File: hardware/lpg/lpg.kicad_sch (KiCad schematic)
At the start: 66 parts, among them J1 AudioJack2_SwitchT, J2 AudioJack2_SwitchT, J3 AudioJack2_SwitchT, J4 AudioJack2_SwitchT, J5 Conn_02x05_Odd_Even, Q1 BC547, Q2 BC547, SW1 SW_3PDT_x3, SW2 SW_DPDT_x2, U1 TL074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

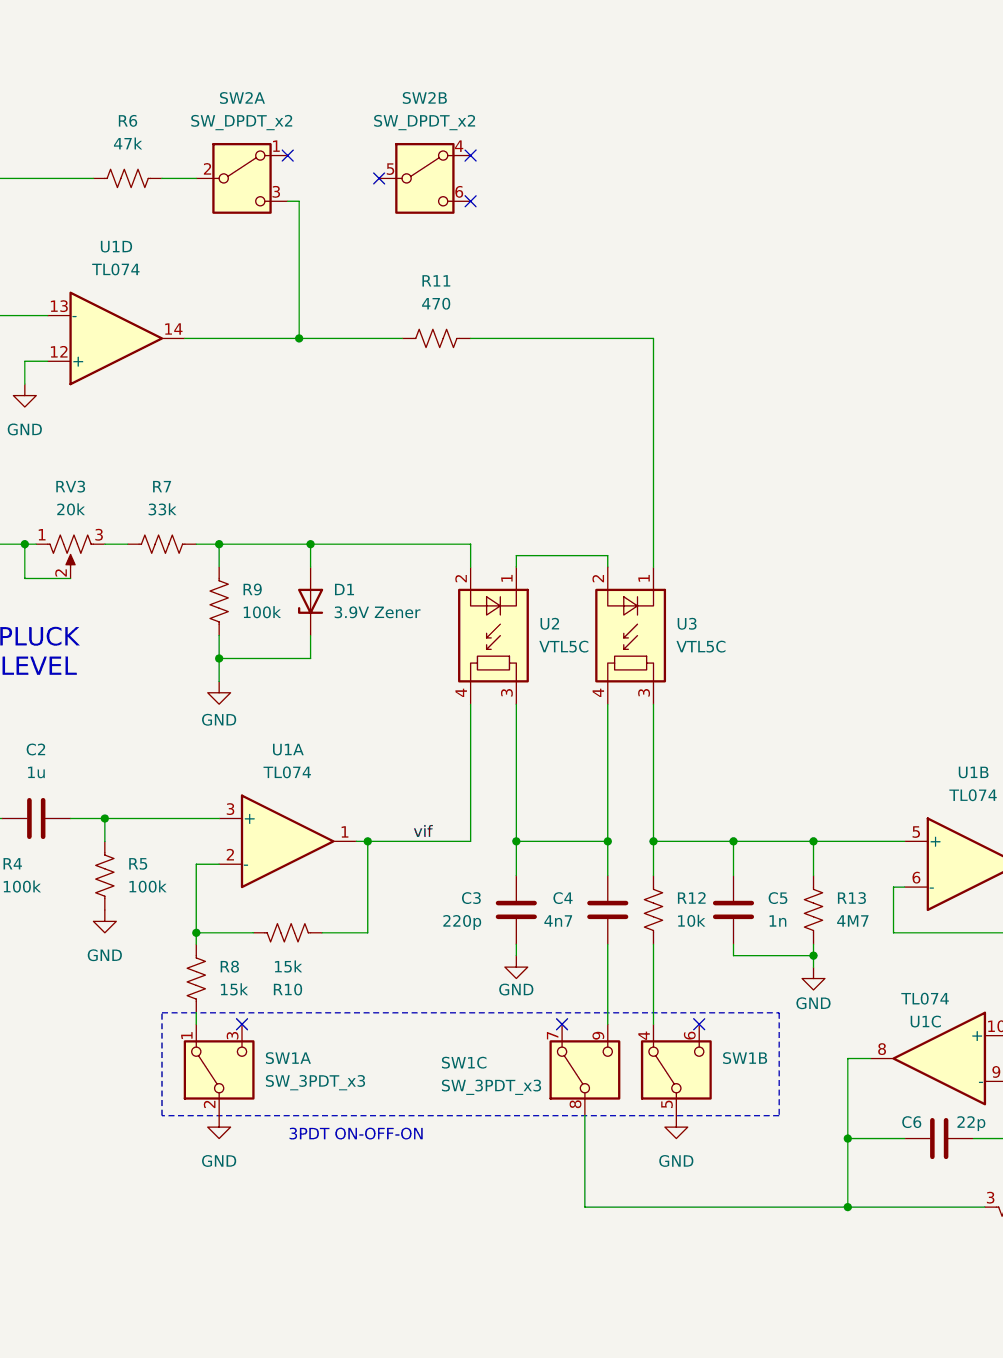
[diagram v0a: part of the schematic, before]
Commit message: replaced switches with 4P3T slider and SPDT M5 sub-mini toggle
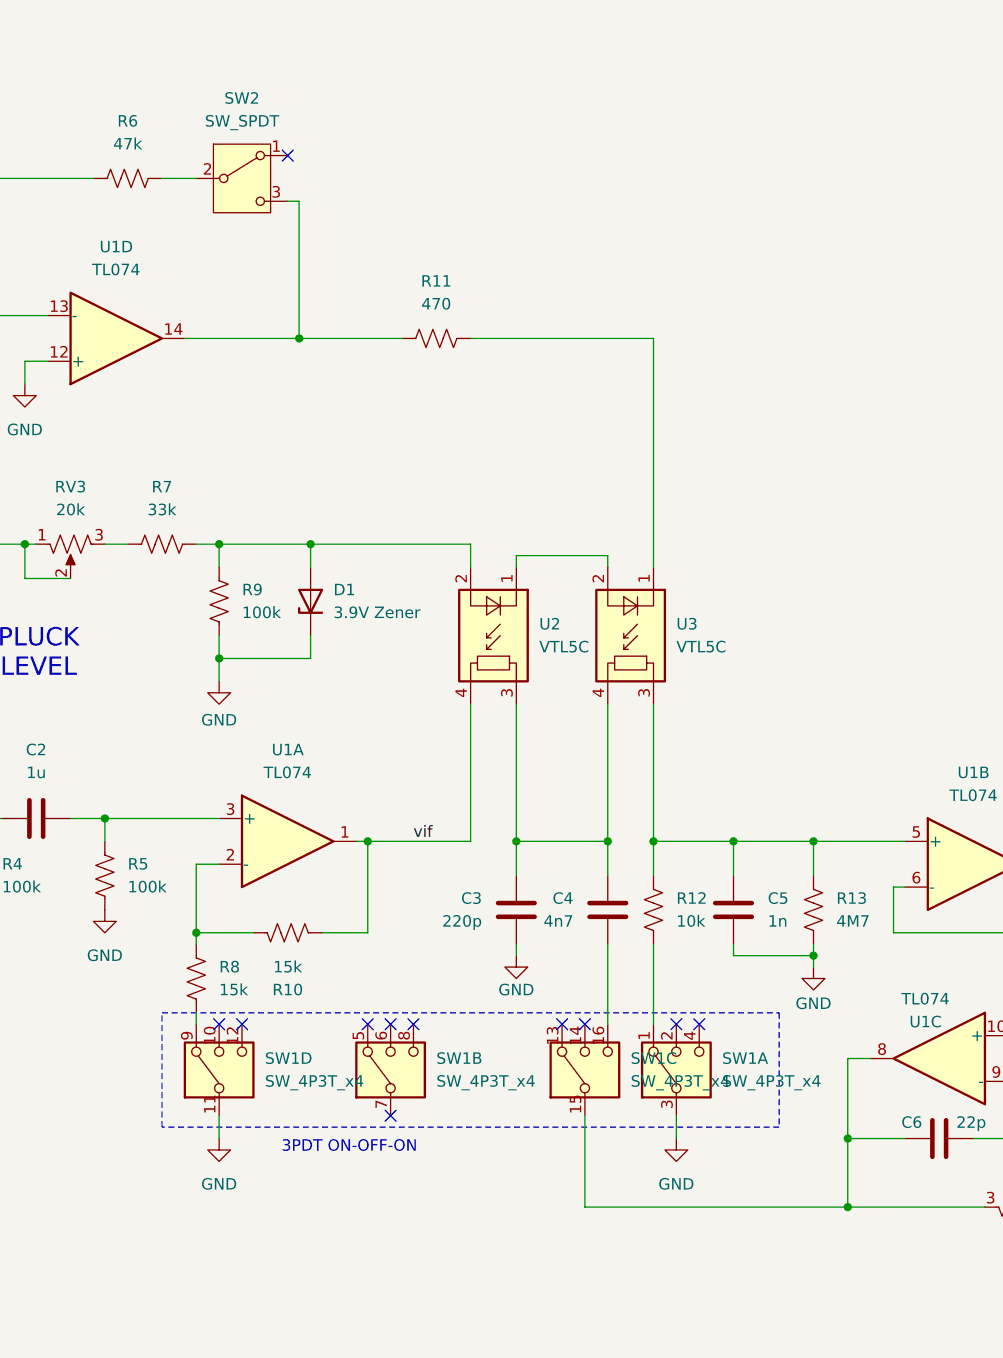
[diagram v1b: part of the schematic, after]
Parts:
- removed SW1: SW_3PDT_x3, Switches:SW_3PDT_18mm_x_13mm_P4.50mm, symbol Modular_Switches:SW_3PDT_x3
- removed SW2: SW_DPDT_x2, Switches:SW_DPDT_13mm_x_13mm_P5.00mm, symbol Switch:SW_DPDT_x2
- added SW1: SW_4P3T_x4, Switches:SW_4P3T_SS-43D01_NoFrame, symbol Modular_Switches:SW_4P3T_x4
- added SW2: SW_SPDT, Switches:SW_Dailywell_SPDT_2MS1T1B1M1, symbol Switch:SW_SPDT
- C5: footprint Capacitor_THT:C_Disc_D5.0mm_W2.5mm_P2.50mm -> Capacitor_THT:C_Disc_D5.0mm_W2.5mm_P5.00mm
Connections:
- net GND: now also SW1.11, SW1.3
- net at C4.1: now also SW1.16
- net at C6.2, RV4.3, U1.8: now also SW1.15
- net at R11.2, U1.14: now also SW2.3 (C)
- net at R8.2: now also SW1.9
- net at R12.2: now also SW1.1
- net at R6.1: now also SW2.2 (B)
- no-connect marks 11 -> 15

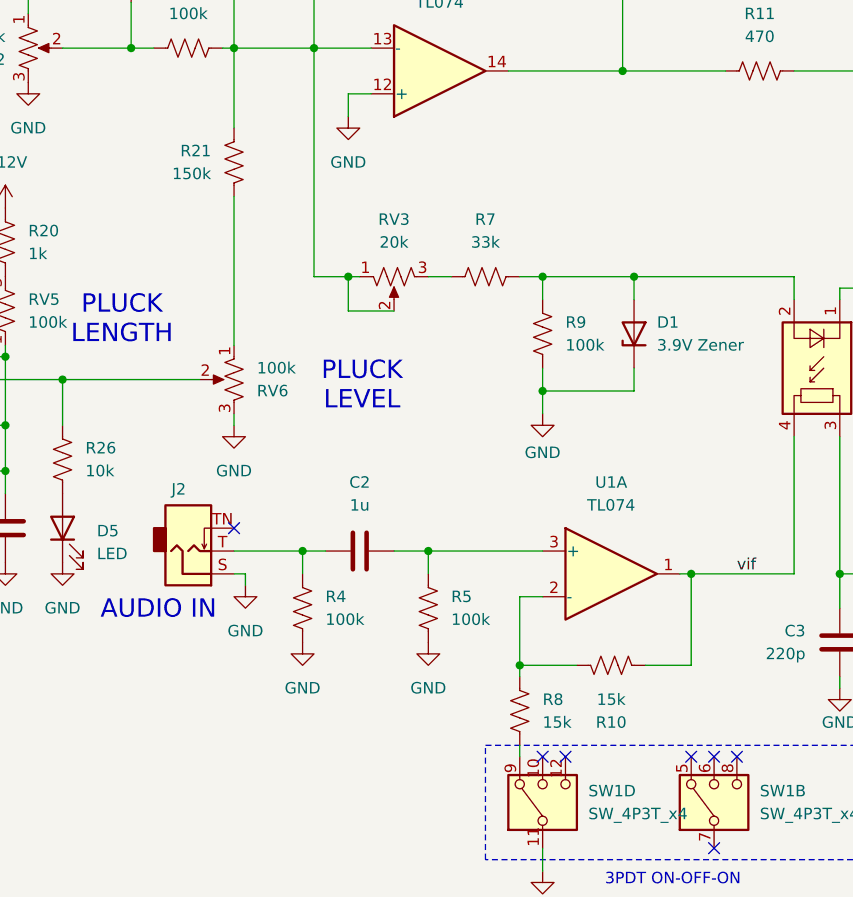
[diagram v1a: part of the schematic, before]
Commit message: Faceplate layout and silkscreen
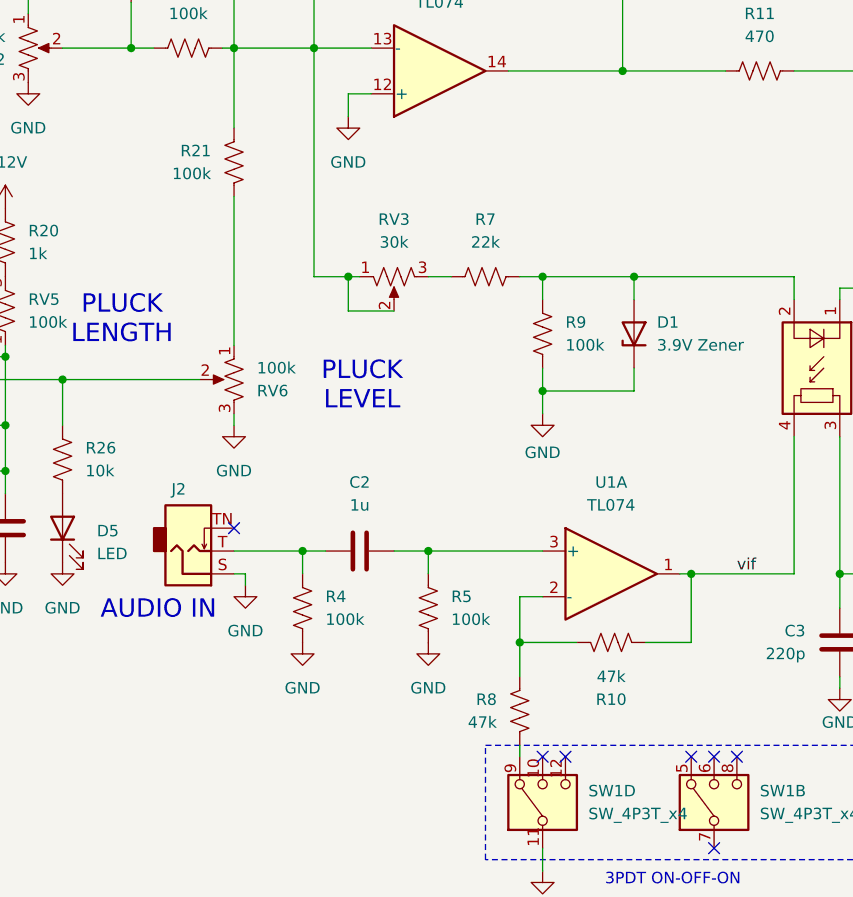
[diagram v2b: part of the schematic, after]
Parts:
- R10, R8: value 15k -> 47k
- R21: value 150k -> 100k
- R7: value 33k -> 22k
- RV3: value 20k -> 30k
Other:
- moved on the sheet: R10
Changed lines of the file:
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@@
 	)
 	(junction
+		(at 160.02 111.76)
+		(diameter 0)
+		(color 0 0 0 0)
+	)
+	(junction
 		(at 102.87 87.63)
 		(diameter 0)
@@
 	)
 	(junction
-		(at 160.02 114.3)
-		(diameter 0)
-		(color 0 0 0 0)
-	)
-	(junction
 		(at 90.17 154.94)
 		(diameter 0)
@@
 	(wire
 		(pts
-			(xy 160.02 114.3) (xy 160.02 115.57)
+			(xy 160.02 111.76) (xy 160.02 115.57)
 		)
 		(stroke
@@
 	(wire
 		(pts
-			(xy 160.02 114.3) (xy 166.37 114.3)
+			(xy 160.02 111.76) (xy 166.37 111.76)
 		)
 		(stroke
@@
 	(wire
 		(pts
-			(xy 179.07 114.3) (xy 179.07 104.14)
+			(xy 179.07 111.76) (xy 179.07 104.14)
 		)
 		(stroke
@@
 	(wire
 		(pts
-			(xy 160.02 106.68) (xy 160.02 114.3)
+			(xy 160.02 106.68) (xy 160.02 111.76)
 		)
 		(stroke
@@
 	(wire
 		(pts
-			(xy 173.99 114.3) (xy 179.07 114.3)
+			(xy 173.99 111.76) (xy 179.07 111.76)
 		)
 		(stroke
@@
 	(symbol
 		(lib_id "Device:R_US")
-		(at 170.18 114.3 90)
+		(at 170.18 111.76 90)
 		(mirror x)
 		(unit 1)
@@
 		(dnp no)
 		(property "Reference" "R10"
-			(at 170.18 120.65 90)
+			(at 170.18 118.11 90)
 			(effects
 				(font
@@
 			)
 		)
-		(property "Value" "15k"
-			(at 170.18 118.11 90)
+		(property "Value" "47k"
+			(at 170.18 115.57 90)
 			(effects
 				(font
@@
 		)
 		(property "Footprint" "Resistor_THT:R_Axial_DIN0204_L3.6mm_D1.6mm_P2.54mm_Vertical"
-			(at 170.434 115.316 90)
+			(at 170.434 112.776 90)
 			(effects
 				(font
@@
 		)
 		(property "Datasheet" "~"
-			(at 170.18 114.3 0)
+			(at 170.18 111.76 0)
 			(effects
 				(font
@@
 		)
 		(property "Description" "Resistor, US symbol"
-			(at 170.18 114.3 0)
+			(at 170.18 111.76 0)
 			(effects
 				(font
@@
 		(lib_id "Device:R_US")
 		(at 160.02 119.38 0)
+		(mirror y)
 		(unit 1)
 		(exclude_from_sim no)
@@
 		(on_board yes)
 		(dnp no)
-		(fields_autoplaced yes)
 		(property "Reference" "R8"
-			(at 162.56 118.1099 0)
+			(at 157.48 118.1099 0)
 			(effects
 				(font
@@
 			)
 		)
-		(property "Value" "15k"
-			(at 162.56 120.6499 0)
+		(property "Value" "47k"
+			(at 157.48 120.6499 0)
 			(effects
 				(font
@@
 		)
 		(property "Footprint" "Resistor_THT:R_Axial_DIN0204_L3.6mm_D1.6mm_P2.54mm_Vertical"
-			(at 161.036 119.634 90)
+			(at 159.004 119.634 90)
 			(effects
 				(font
@@
 			)
 		)
-		(property "Value" "150k"
+		(property "Value" "100k"
 			(at 125.73 59.6899 0)
 			(effects
@@
 			)
 		)
-		(property "Value" "20k"
+		(property "Value" "30k"
 			(at 146.05 67.31 90)
 			(effects
@@
 			)
 		)
-		(property "Value" "33k"
+		(property "Value" "22k"
 			(at 156.21 67.31 90)
 			(effects

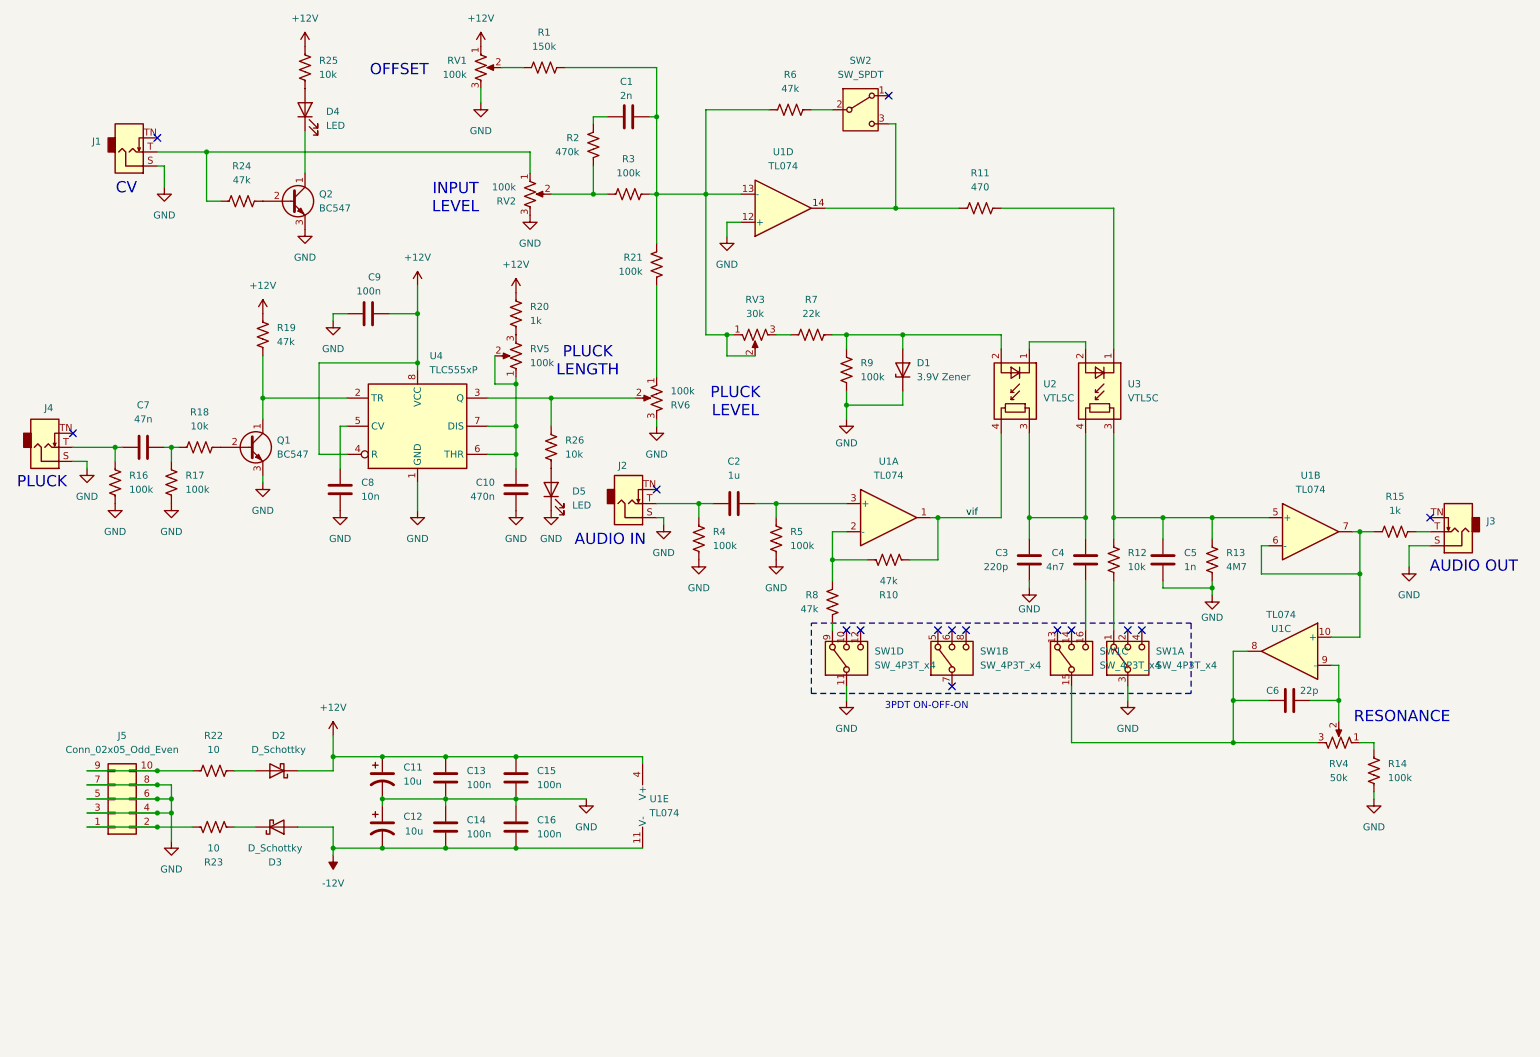
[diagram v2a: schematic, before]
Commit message: Update KiCad project settings and error handling parameters
- Added new error handling for "creepage", "hole_to_hole", "text_on_edge_cuts", "track_angle", and "track_segment_length".
- Set "footprint_filters_mismatch" and "footprint_type_mismatch" to "ignore".
- Updated teardrop options to include "td_onpthpad" and "td_onsmdpad".
- Introduced "min_groove_width" parameter.
- Adjusted version numbers in meta information.
- Added "priority" field to net settings.
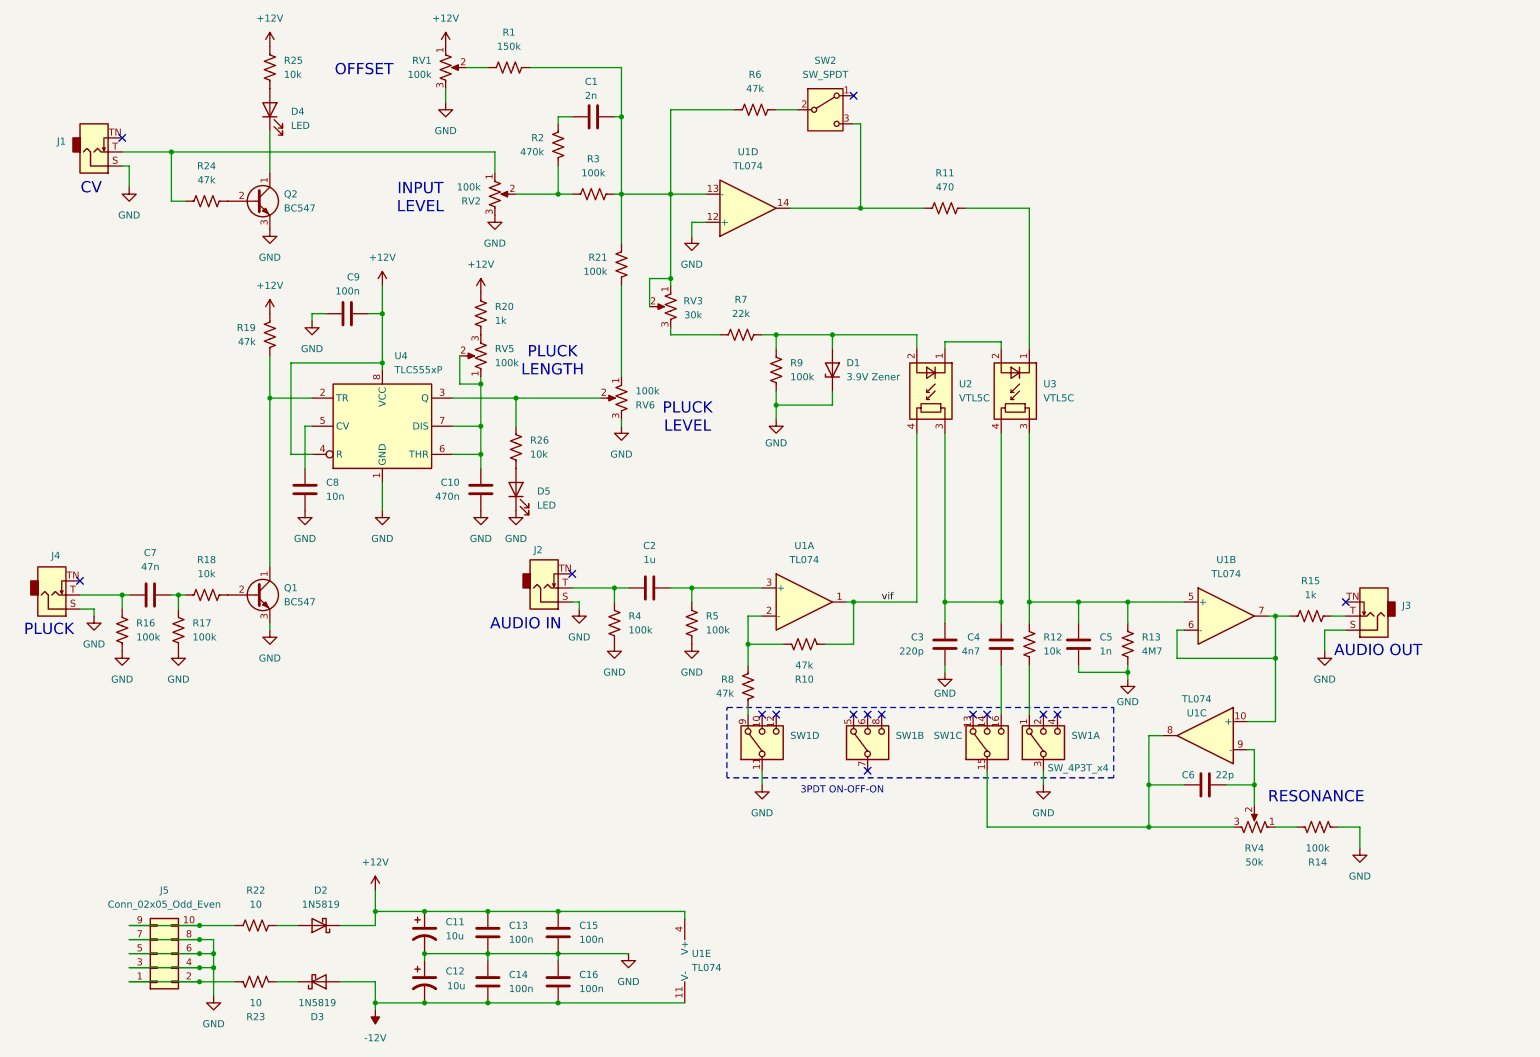
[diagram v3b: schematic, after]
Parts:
- D2, D3: value D_Schottky -> 1N5819
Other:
- moved on the sheet: C1, C10, C11, C12, C13, C14, C15, C16, C2, C3, C4, C5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
